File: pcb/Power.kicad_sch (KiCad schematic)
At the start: 94 parts, among them J5 Barrel_Jack, Q2 ZXMC3A16DN8, U2 LFE5U-85F-6BG381, U8 LTC4360-2, U9 LTM8051

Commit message: Rough PCB component placement
- This will change
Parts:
- removed C108, C99: 100u, Capacitor_SMD:C_0402_1005Metric, symbol Device:C
- removed C113: 22u, Capacitor_SMD:C_1210_3225Metric, symbol Device:C
- removed C115, C62, C77, C78: 100u, Capacitor_Tantalum_SMD:CP_EIA-3216-18_Kemet-A, symbol Device:C
- removed C116, C117, C118, C119: 1u, Capacitor_SMD:C_0805_2012Metric, symbol Device:C
- removed C123, C129, C92: 100n, Capacitor_SMD:C_0402_1005Metric, symbol Device:C
- removed C130: 10n, Capacitor_SMD:C_0402_1005Metric, symbol Device:C
- removed D11: GBLC08C, Diode_SMD:D_SOD-323, symbol Device:D_Zener_Dual_CommonAnode_KAK
- removed J5: Barrel_Jack, Connector_BarrelJack:BarrelJack_Horizontal, symbol Connector:Barrel_Jack
- added C103: 100u, Capacitor_Tantalum_SMD:CP_EIA-6032-15_Kemet-U_Pad2.25x2.35mm_HandSolder, symbol Device:C
- added C104, C122, C126: 1u, Capacitor_SMD:C_0603_1608Metric, symbol Device:C
- added C121, C124, C125, C127, C128: 100u, Capacitor_SMD:C_0805_2012Metric, symbol Device:C
- added C98: 22u, Capacitor_SMD:C_1210_3225Metric, symbol Device:C
- added D11: GBLC08C, Diode_SMD:D_SOD-323, symbol Device:D_TVS
- added J5: Barrel_Jack_Switch, Connector_BarrelJack:BarrelJack_CUI_PJ-102AH_Horizontal, symbol Connector:Barrel_Jack_Switch
- C105: renamed from C59; footprint Capacitor_SMD:C_0805_2012Metric -> Capacitor_SMD:C_0603_1608Metric
- C107: renamed from C91; footprint Capacitor_SMD:C_1210_3225Metric -> Capacitor_SMD:C_0805_2012Metric
- C111: renamed from C96; footprint Capacitor_SMD:C_1210_3225Metric -> Capacitor_SMD:C_0805_2012Metric
- C115: renamed from C104; footprint Capacitor_SMD:C_1210_3225Metric -> Capacitor_SMD:C_0805_2012Metric
- C120: renamed from C61; footprint Capacitor_Tantalum_SMD:CP_EIA-3216-18_Kemet-A -> Capacitor_SMD:C_0805_2012Metric; Voltage (none) -> 4V
- C130: renamed from C110; value 22p -> 10p
- C131: renamed from C111; value 10p -> 22p
- C64: renamed from C121; footprint Capacitor_SMD:C_1210_3225Metric -> Capacitor_SMD:C_0805_2012Metric
- C69: renamed from C126; footprint Capacitor_SMD:C_0402_1005Metric -> Capacitor_SMD:C_0805_2012Metric
- C75: renamed from C64; footprint Capacitor_SMD:C_1210_3225Metric -> Capacitor_SMD:C_0805_2012Metric
- C76: renamed from C65; footprint Capacitor_SMD:C_1210_3225Metric -> Capacitor_SMD:C_0805_2012Metric
- C88: renamed from C80; footprint Capacitor_SMD:C_1210_3225Metric -> Capacitor_SMD:C_0805_2012Metric
- C89: renamed from C81; footprint Capacitor_SMD:C_0805_2012Metric -> Capacitor_SMD:C_0603_1608Metric
- C94: renamed from C86; footprint Capacitor_SMD:C_1210_3225Metric -> Capacitor_SMD:C_0805_2012Metric
- C99: renamed from C100; footprint Capacitor_SMD:C_1210_3225Metric -> Capacitor_SMD:C_0805_2012Metric
- U8: footprint Package_SO:SO-8_3.9x4.9mm_P1.27mm -> Package_TO_SOT_SMD:SC-70-8
- renumbered C101 to C100, C102 to C101, C103 to C102, C90 to C106, C93 to C108, C94 to C109, C95 to C110, C97 to C112, C98 to C113, C105 to C116, C106 to C117, C107 to C118, C60 to C119, C76 to C123, C109 to C129, C112 to C132, C120 to C63, C122 to C65, C124 to C67, C125 to C68, C127 to C70, C128 to C71, C131 to C72, C132 to C73, C63 to C74, C66 to C77, C67 to C78, C68 to C79, C69 to C80, C70 to C81, C71 to C82, C72 to C83, C73 to C84, C74 to C85, C75 to C86, C79 to C87, C82 to C90, C83 to C91, C84 to C92, C85 to C93, C87 to C95, C88 to C96, C89 to C97, R44 to R41, R45 to R42, R46 to R43, R47 to R44, R52 to R45, R50 to R46, R53 to R47, R51 to R48, R48 to R49, R49 to R50, U2 to U1
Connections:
- net +1V1: now also C121.1
- net +2V5: now also U9.B1 (VOUT_{3}), C128.1; no longer U9., U9.B3 (VOUT_{3})
- net +3V3: now also C127.1
- net +5V: now also C103.1, C104.1, C122.1, C126.1
- net GND: now also C103.2, C104.2, C121.2, C122.2, C124.2, C125.2, C126.2, C127.2, C128.2, C98.2, D11.1 (A1), J5.2, J5.3
- net RAM_VDD: now also C124.1, C125.1
- net VCCIO3: now also C98.1
- net at Q2.5 (D), Q2.6 (D): now also D11.2 (A2), J5.1
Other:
- note added: "1.2 MHz"
- note added: "800 kHz"
- note added: "Default: 1.35V"
- note added: "FPGA Power"
- note added: "Power Regulation"
- note removed: "default 1.35V"
- moved on the sheet: C100, C101, C102, C105, C106, C107, C108, C109, C110, C111, C112, C113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

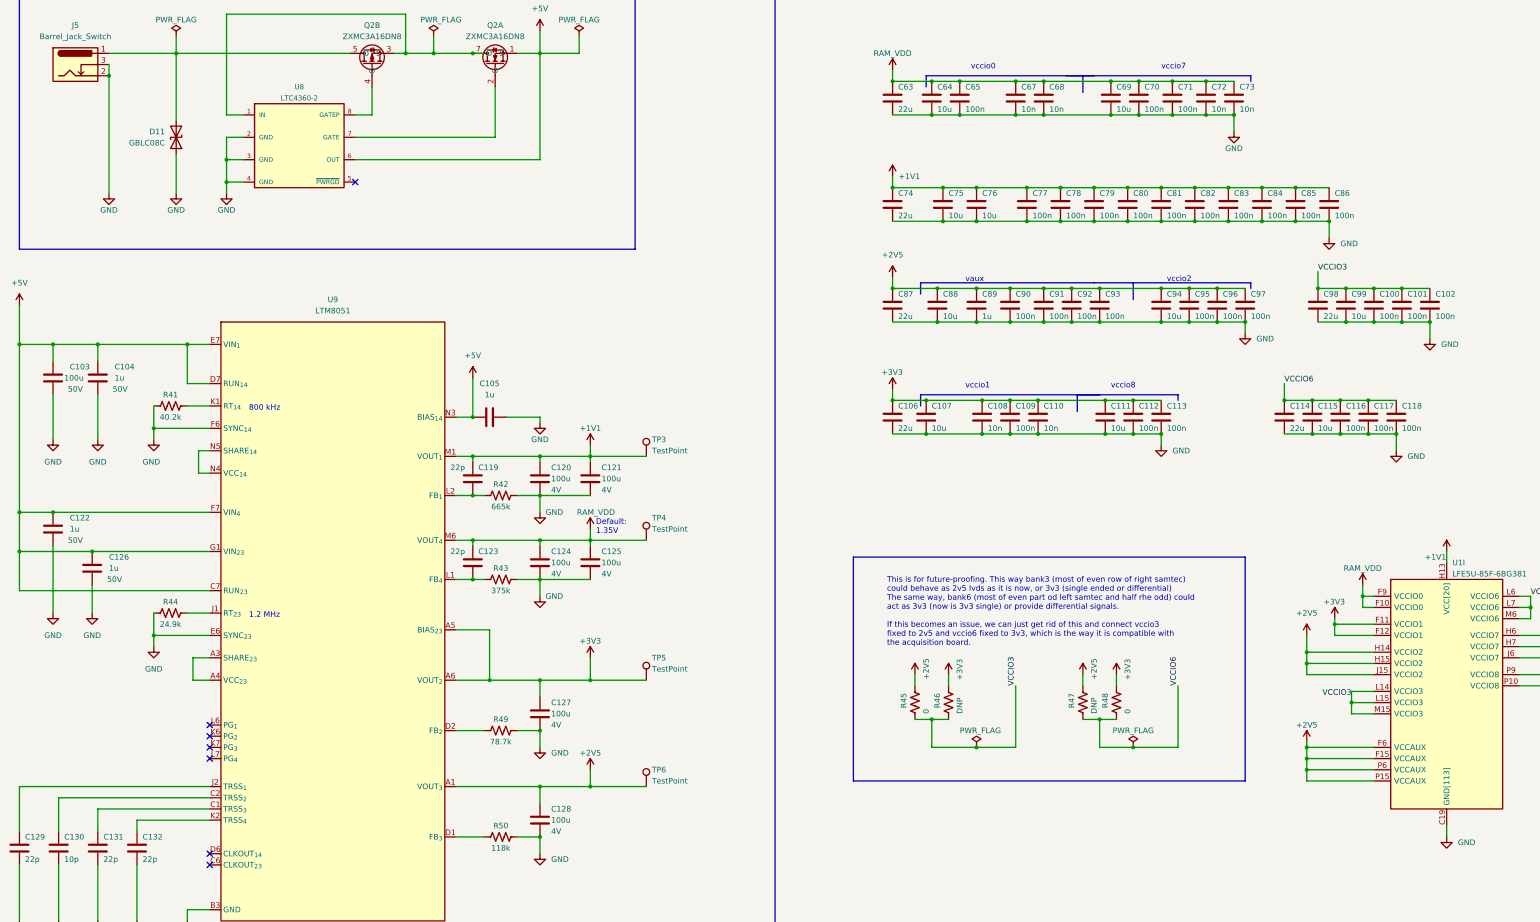
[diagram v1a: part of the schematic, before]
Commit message: Performed rough RAM routing
- Traces 25 mm long, all matched.
- No power routed yet but I want to confirm that FPGA pin remap before
going forward because I can probably make this work.
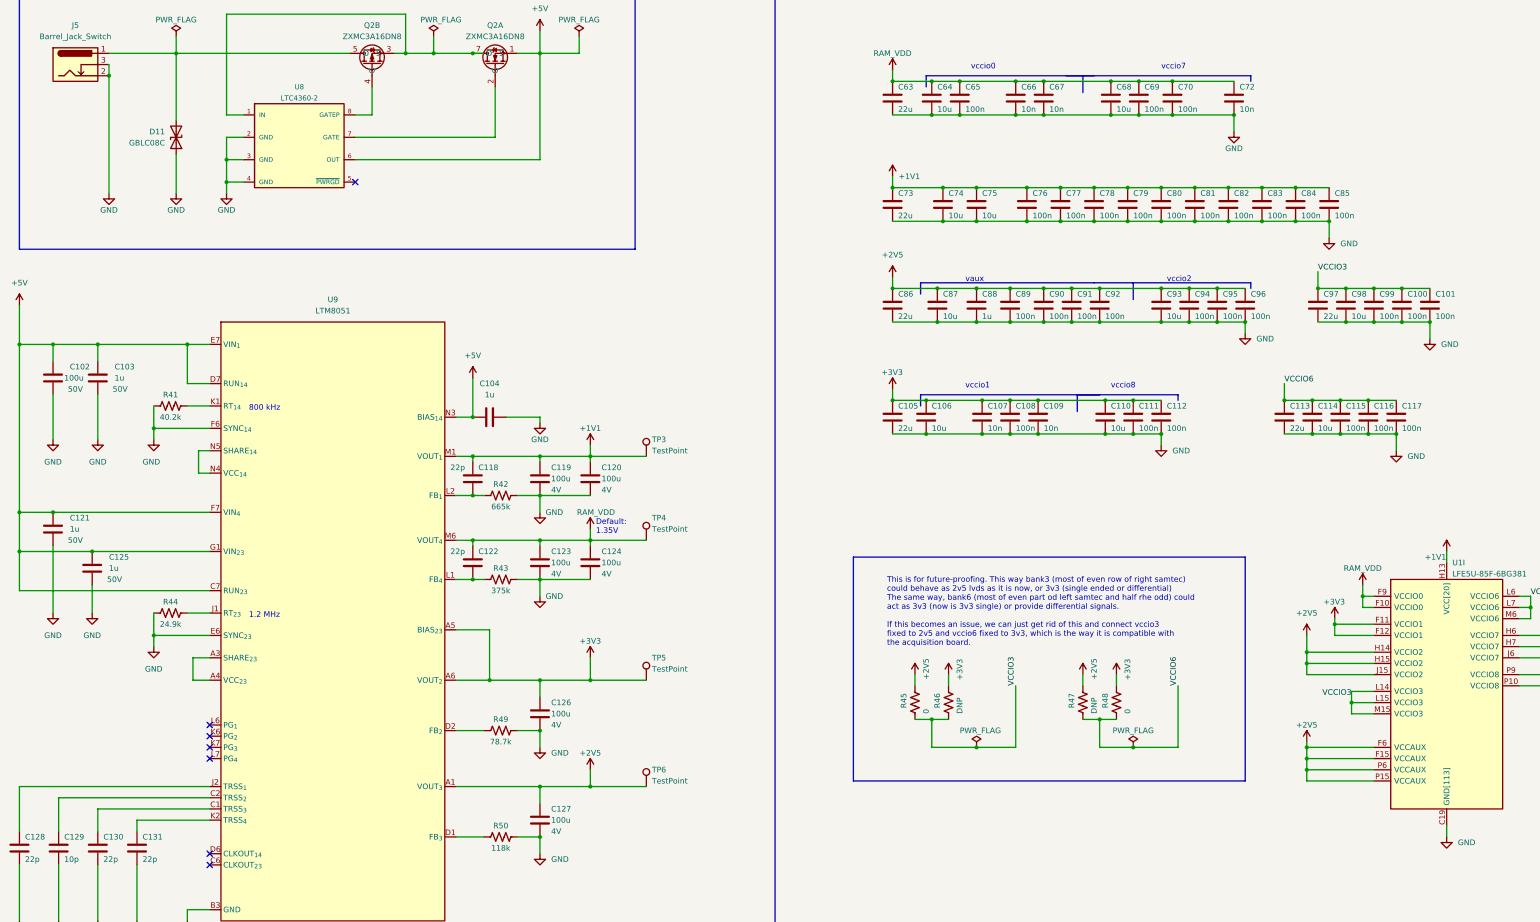
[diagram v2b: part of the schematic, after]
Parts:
- removed C72: 10n, Capacitor_SMD:C_0402_1005Metric, symbol Device:C
- renumbered C101 to C100, C102 to C101, C103 to C102, C104 to C103, C105 to C104, C106 to C105, C107 to C106, C108 to C107, C109 to C108, C110 to C109, C111 to C110, C112 to C111, C113 to C112, C114 to C113, C115 to C114, C116 to C115, C117 to C116, C118 to C117, C119 to C118, C120 to C119, C121 to C120, C122 to C121, C123 to C122, C124 to C123, C125 to C124, C126 to C125, C127 to C126, C128 to C127, C129 to C128, C130 to C129, C131 to C130, C132 to C131, C67 to C66, C68 to C67, C69 to C68, C70 to C69, C71 to C70, C73 to C72, C74 to C73, C75 to C74, C76 to C75, C77 to C76, C78 to C77, C79 to C78, C80 to C79, C81 to C80, C82 to C81, C83 to C82, C84 to C83, C85 to C84, C86 to C85, C87 to C86, C88 to C87, C89 to C88, C90 to C89, C91 to C90, C92 to C91, C93 to C92, C94 to C93, C95 to C94, C96 to C95, C97 to C96, C98 to C97, C99 to C98, C100 to C99

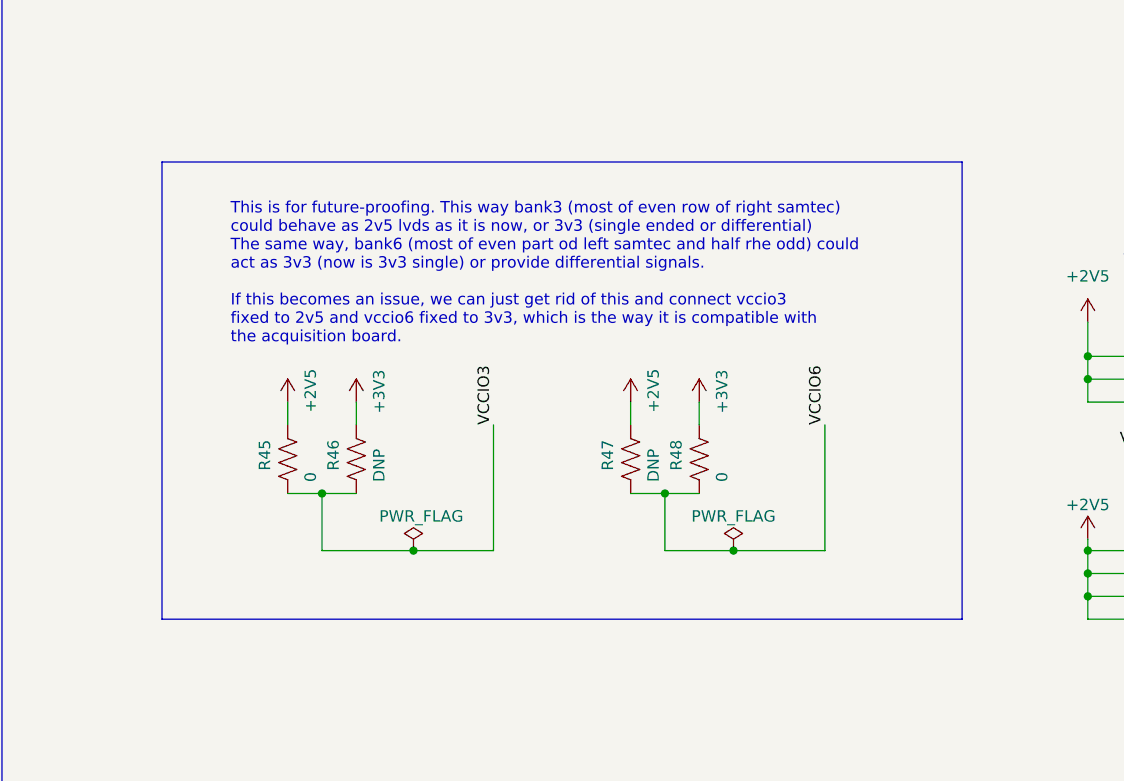
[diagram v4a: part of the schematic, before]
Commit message: Finished IO pin swaping and most of routing
- Left connector is done, includeing trace tuning
- Right conenctor is layed out but needs length tuning
- Decided to move FTDI closer to FPGA and I'm in the middle of that
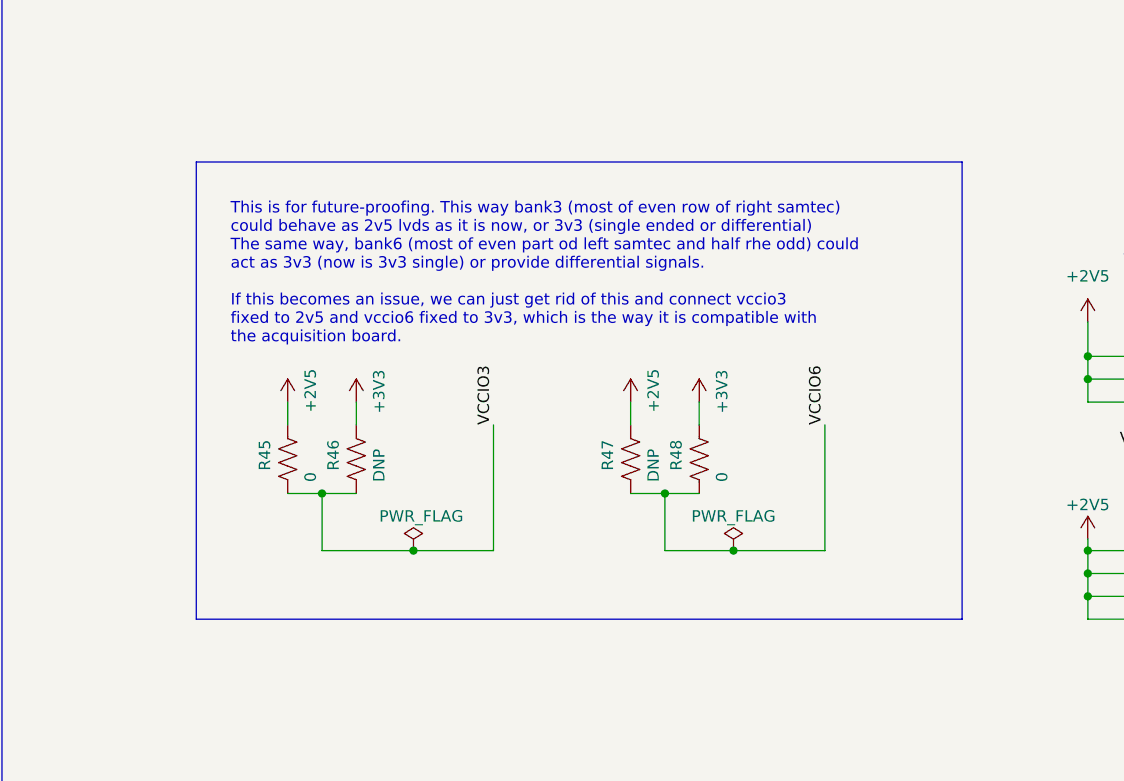
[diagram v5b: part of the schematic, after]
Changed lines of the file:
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@@
     (stroke (width 0) (type default) (color 0 0 0 0))
   )
-  (polyline (pts (xy 318.77 210.82) (xy 229.87 210.82))
+  (polyline (pts (xy 318.77 210.82) (xy 233.68 210.82))
     (stroke (width 0) (type default) (color 0 0 0 0))
   )
@@
     (stroke (width 0) (type default) (color 0 0 0 0))
   )
-  (polyline (pts (xy 229.87 160.02) (xy 229.87 210.82))
+  (polyline (pts (xy 233.68 160.02) (xy 233.68 210.82))
     (stroke (width 0) (type default) (color 0 0 0 0))
   )
@@
     (stroke (width 0) (type default) (color 0 0 0 0))
   )
-  (polyline (pts (xy 229.87 160.02) (xy 318.77 160.02))
-    (stroke (width 0) (type default) (color 0 0 0 0))
-  )
+  (polyline (pts (xy 233.68 160.02) (xy 318.77 160.02))
+    (stroke (width 0) (type default) (color 0 0 0 0))
+  )
